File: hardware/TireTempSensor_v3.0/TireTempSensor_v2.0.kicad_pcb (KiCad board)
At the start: 4 copper layers, 81.5 x 20.6 mm, 89 parts, among them IC2 MLX90621ESF-BAB-000-SP, IC4 TPS54202HDDCR, J3 FTSH-107-01-L-D-K, T10 TP_+5V, T14 TP_+3.3V, T15 TP_+2.6V, U1 STM32G0C1KCTxN, U2 MIC5306-2.6YD5-TR, U3 NCP715SQ33T2G, U7 ADM3057ExRW, Y1 ATX-11-F-32.000MHZ-F05-T

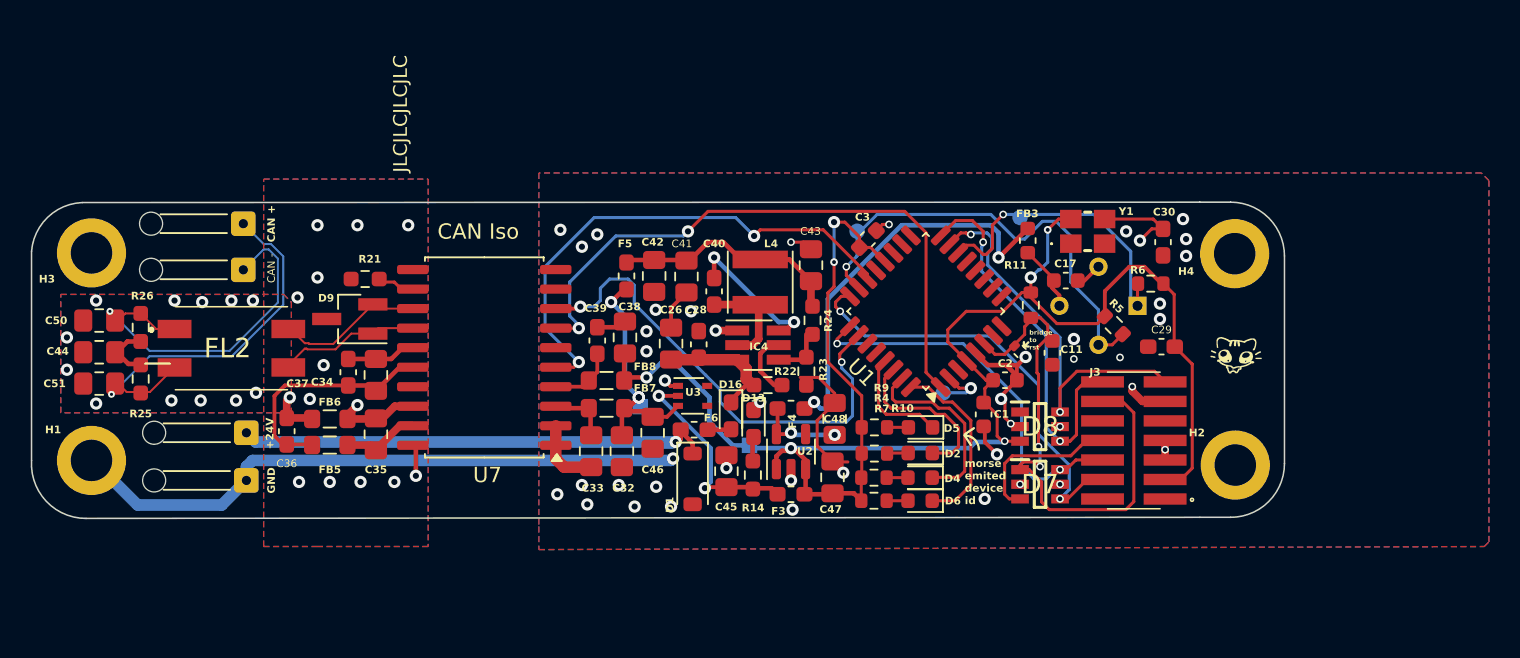
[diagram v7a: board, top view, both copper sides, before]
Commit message: Zmieniono ldo na 3.3V, dodano linki do mousera, gotowe na relase
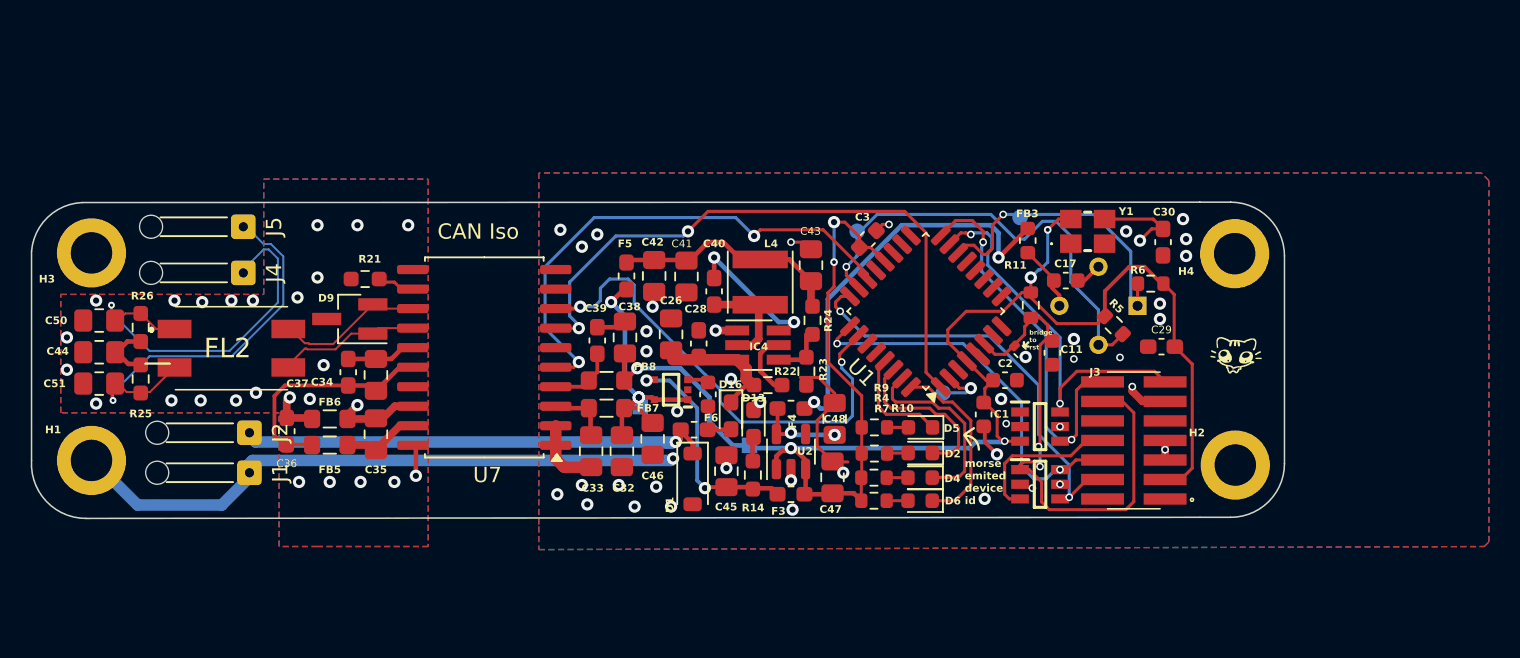
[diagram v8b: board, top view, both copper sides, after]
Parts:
- removed +24V, GND: Conn_01x01, Connector_Wire:SolderWire-0.1sqmm_1x01_D0.4mm_OD1mm_Relief
- removed CAN +: Conn_01x01, Connector_Wire:SolderWire-0.1sqmm_1x01_D0.4mm_OD1mm_Relief
- removed CAN -: Conn_01x01, Connector_Wire:SolderWire-0.1sqmm_1x01_D0.4mm_OD1mm_Relief
- removed U3: NCP715SQ33T2G, Package_TO_SOT_SMD:SOT-353_SC-70-5
- added C31: 100n, Capacitor_SMD:C_0603_1608Metric, F.Cu at (133.0, 101.5)
- added IC1: TAR5S33UTE85LF, footprint:SOTFL65P210X75-5N, F.Cu at (130.6, 101.2)
- added J1: Conn_01x01, Connector_Wire:SolderWire-0.1sqmm_1x01_D0.4mm_OD1mm_Relief, F.Cu at (103.2, 106.6)
- added J2: Conn_01x01, Connector_Wire:SolderWire-0.1sqmm_1x01_D0.4mm_OD1mm_Relief, F.Cu at (103.2, 104.0)
- added J4: Conn_01x01, Connector_Wire:SolderWire-0.1sqmm_1x01_D0.4mm_OD1mm_Relief, F.Cu at (102.8, 93.6)
- added J5: Conn_01x01, Connector_Wire:SolderWire-0.1sqmm_1x01_D0.4mm_OD1mm_Relief, F.Cu at (102.8, 90.6)
- C44: value 4.7n -> 1p
- moved C26 0.60 mm to (130.6, 97.6)
- moved C46 0.40 mm to (129.4, 104.4)
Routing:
- net GND: track 82.6 -> 69.8 mm
- net +5V: track 14.4 -> 16.7 mm
- net Net-(IC1-NOISE): track 0.00 -> 1.39 mm
- net /Power Supply 3.3v 2.6v/VO_+3.3V: track 13.7 -> 15.0 mm
- net /SWDIO: track 27.5 -> 26.5 mm
- net /CAN+: track 25.8 -> 26.6 mm
- net /CAN-: track 24.5 -> 25.2 mm
- net /URAT_RX: track 25.8 -> 25.2 mm
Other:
- board text removed: "JLCJLCJLCJLC"
